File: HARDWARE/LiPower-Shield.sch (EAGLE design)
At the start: 42 parts, among them U1 MAX17043G+U, U2 TPS61200, U3 MCP73831, U4 ARDUINO_SHIELDNOLABELS, X1 USBSMD

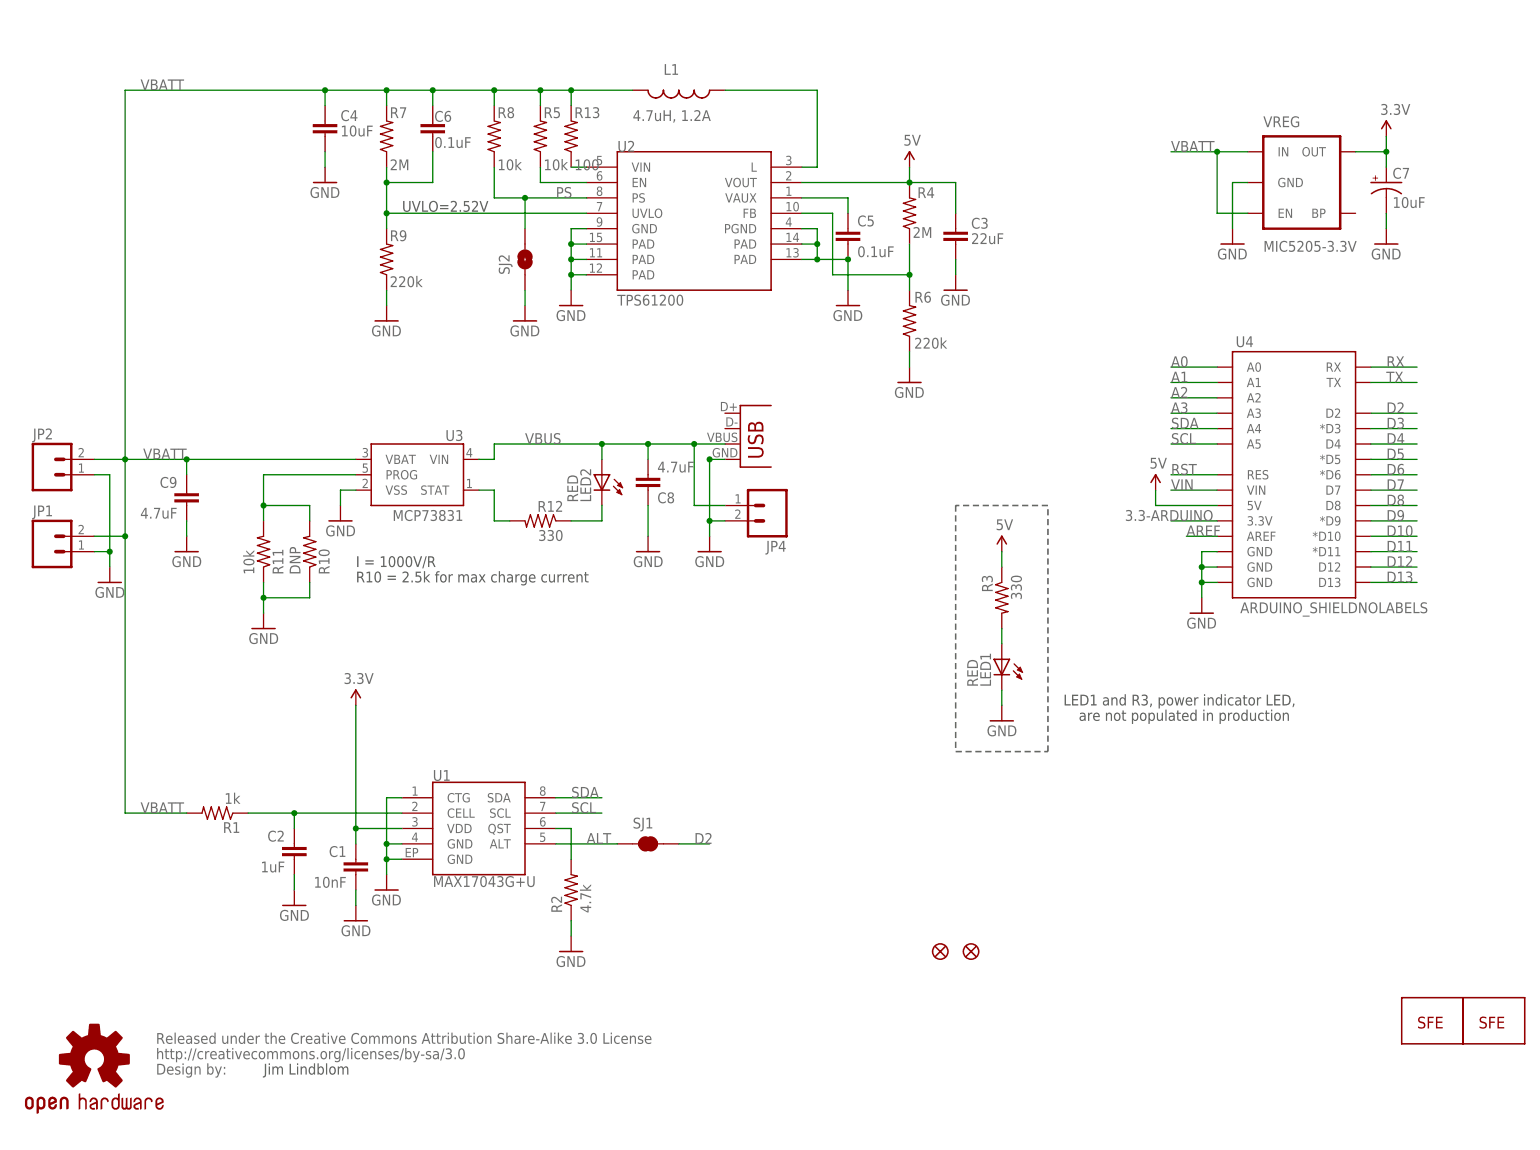
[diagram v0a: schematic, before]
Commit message: Had to re-commit original files
The v13 files that I pulled from the network are not what we have on
storefront. commited v12,  also from the network, seems to be the same
as the SF product.
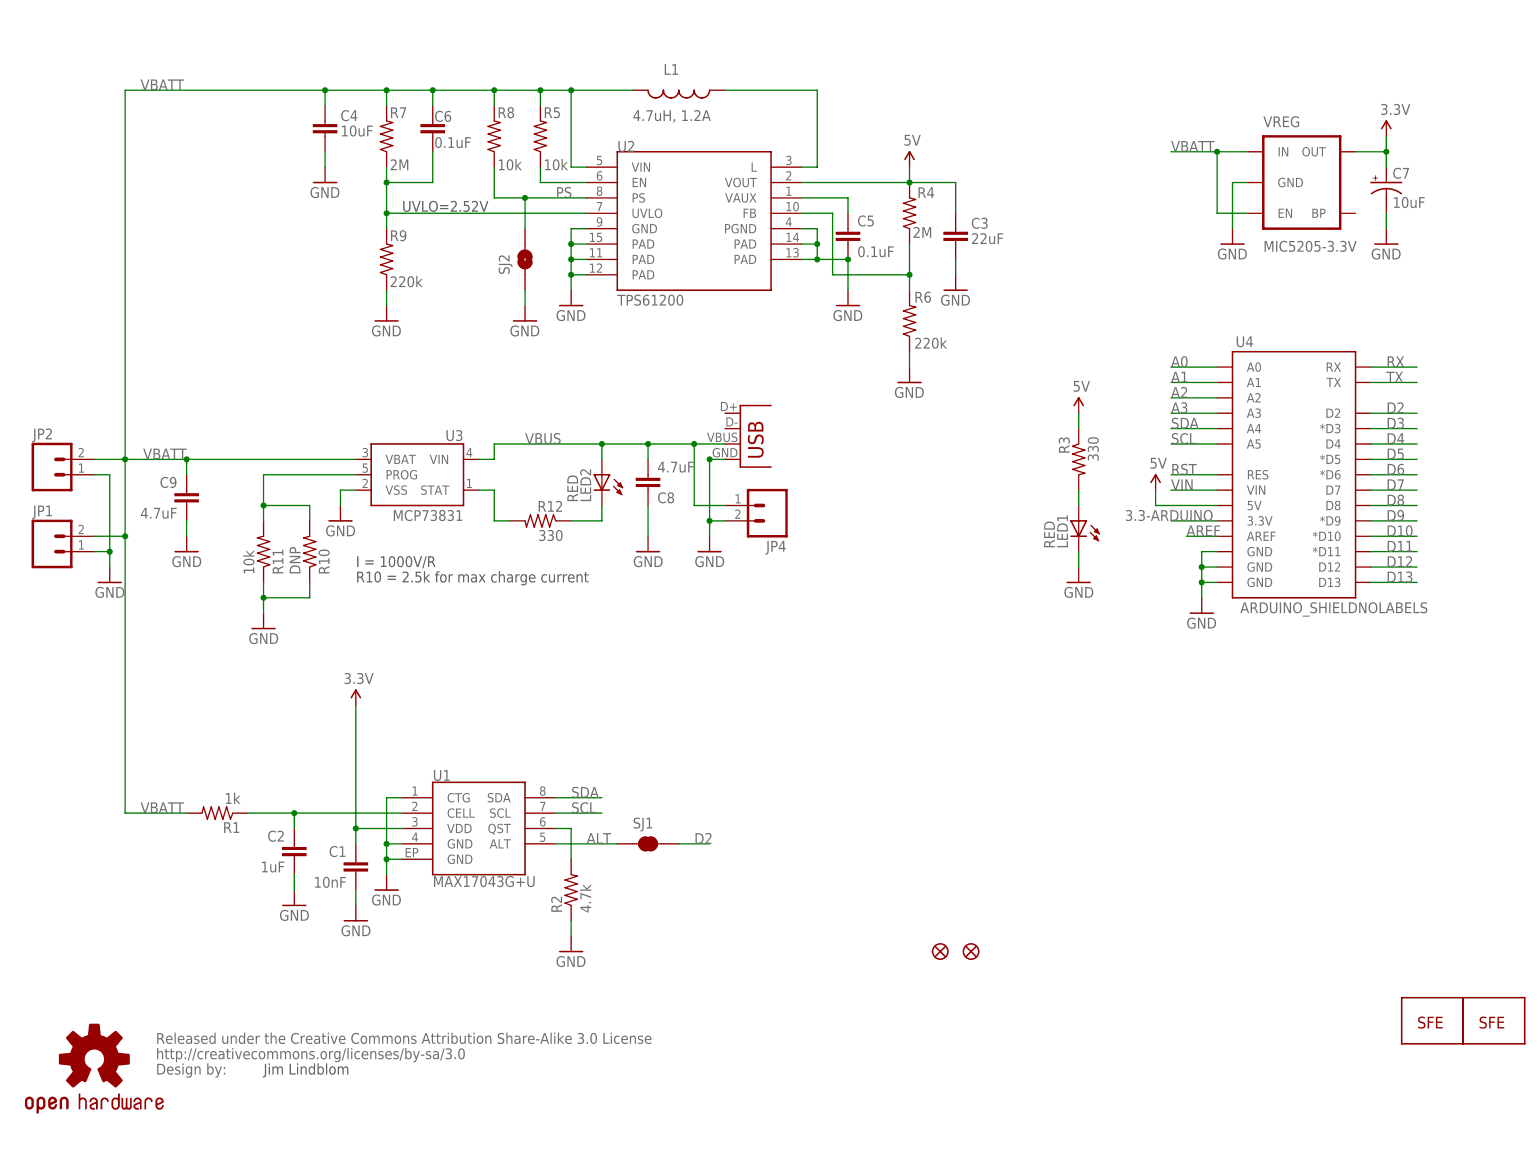
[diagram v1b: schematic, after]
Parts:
- removed R13: 100, SparkFun:RESISTOR0402-RES
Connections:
- removed net VIN-L: R13.1, U2.VIN
- net VBATT: now also U2.VIN; no longer R13.2
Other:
- note removed: "LED1 and R3, power indicator LED,"
- note removed: "are not populated in production"
- moved on the sheet: LED1, R3
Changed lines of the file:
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@@
 <part name="JP5" library="abes" deviceset="FIDUCIAL" device="1X2.5"/>
 <part name="JP6" library="abes" deviceset="FIDUCIAL" device="1X2.5"/>
-<part name="R13" library="SparkFun" deviceset="RESISTOR" device="0402-RES" value="100"/>
 </parts>
 <sheets>
@@
 <plain>
 <wire x1="103.124" y1="48.26" x2="105.156" y2="48.26" width="1.27" layer="94"/>
-<wire x1="154.94" y1="104.14" x2="154.94" y2="63.5" width="0.254" layer="97" style="shortdash"/>
-<wire x1="154.94" y1="63.5" x2="170.18" y2="63.5" width="0.254" layer="97" style="shortdash"/>
-<wire x1="170.18" y1="63.5" x2="170.18" y2="104.14" width="0.254" layer="97" style="shortdash"/>
-<wire x1="170.18" y1="104.14" x2="154.94" y2="104.14" width="0.254" layer="97" style="shortdash"/>
 <text x="40.64" y="10.16" size="1.778" layer="97">Jim Lindblom</text>
 <text x="55.88" y="93.98" size="1.778" layer="97">I = 1000V/R</text>
 <text x="55.88" y="91.44" size="1.778" layer="97">R10 = 2.5k for max charge current</text>
 <text x="63.5" y="152.654" size="1.778" layer="97">UVLO=2.52V</text>
-<text x="172.72" y="71.12" size="1.778" layer="97">LED1 and R3, power indicator LED,</text>
-<text x="175.26" y="68.58" size="1.778" layer="97">are not populated in production</text>
 </plain>
 <instances>
@@
 <instance part="C2" gate="G$1" x="45.72" y="45.72" rot="MR0"/>
 <instance part="GND11" gate="1" x="45.72" y="38.1" rot="MR0"/>
-<instance part="LED1" gate="G$1" x="162.56" y="78.74" rot="MR0"/>
-<instance part="R3" gate="G$1" x="162.56" y="88.9" rot="MR270"/>
-<instance part="U$5" gate="G$1" x="162.56" y="96.52"/>
-<instance part="GND14" gate="1" x="162.56" y="68.58" rot="MR0"/>
+<instance part="LED1" gate="G$1" x="175.26" y="101.6" rot="MR0"/>
+<instance part="R3" gate="G$1" x="175.26" y="111.76" rot="MR270"/>
+<instance part="U$5" gate="G$1" x="175.26" y="119.38"/>
+<instance part="GND14" gate="1" x="175.26" y="91.44" rot="MR0"/>
 <instance part="C3" gate="G$1" x="154.94" y="147.32" smashed="yes">
 <attribute name="NAME" x="157.48" y="149.86" size="1.778" layer="95"/>
@@
 <instance part="JP5" gate="G$1" x="152.4" y="30.48"/>
 <instance part="JP6" gate="G$1" x="157.48" y="30.48"/>
-<instance part="R13" gate="G$1" x="91.44" y="165.1" smashed="yes" rot="R90">
-<attribute name="NAME" x="91.948" y="168.1226" size="1.778" layer="95"/>
-<attribute name="VALUE" x="91.948" y="159.512" size="1.778" layer="96"/>
-</instance>
 </instances>
 <busses>
@@
 </segment>
 <segment>
-<wire x1="162.56" y1="71.12" x2="162.56" y2="73.66" width="0.1524" layer="91"/>
+<wire x1="175.26" y1="93.98" x2="175.26" y2="96.52" width="0.1524" layer="91"/>
 <pinref part="LED1" gate="G$1" pin="C"/>
 <pinref part="GND14" gate="1" pin="GND"/>
@@
 </segment>
 <segment>
-<wire x1="162.56" y1="96.52" x2="162.56" y2="93.98" width="0.1524" layer="91"/>
+<wire x1="175.26" y1="119.38" x2="175.26" y2="116.84" width="0.1524" layer="91"/>
 <pinref part="R3" gate="G$1" pin="1"/>
 <pinref part="U$5" gate="G$1" pin="5V"/>
@@
 <wire x1="60.96" y1="170.18" x2="60.96" y2="172.72" width="0.1524" layer="91"/>
 <wire x1="50.8" y1="170.18" x2="50.8" y2="172.72" width="0.1524" layer="91"/>
+<wire x1="50.8" y1="172.72" x2="60.96" y2="172.72" width="0.1524" layer="91"/>
+<wire x1="60.96" y1="172.72" x2="68.58" y2="172.72" width="0.1524" layer="91"/>
+<wire x1="68.58" y1="170.18" x2="68.58" y2="172.72" width="0.1524" layer="91"/>
+<wire x1="68.58" y1="172.72" x2="78.74" y2="172.72" width="0.1524" layer="91"/>
+<wire x1="78.74" y1="172.72" x2="86.36" y2="172.72" width="0.1524" layer="91"/>
+<wire x1="86.36" y1="172.72" x2="91.44" y2="172.72" width="0.1524" layer="91"/>
+<wire x1="101.6" y1="172.72" x2="91.44" y2="172.72" width="0.1524" layer="91"/>
+<wire x1="91.44" y1="172.72" x2="91.44" y2="160.02" width="0.1524" layer="91"/>
+<wire x1="93.98" y1="160.02" x2="91.44" y2="160.02" width="0.1524" layer="91"/>
+<wire x1="78.74" y1="170.18" x2="78.74" y2="172.72" width="0.1524" layer="91"/>
 <wire x1="27.94" y1="53.34" x2="17.78" y2="53.34" width="0.1524" layer="91"/>
-<wire x1="12.7" y1="99.06" x2="17.78" y2="99.06" width="0.1524" layer="91"/>
-<wire x1="17.78" y1="99.06" x2="17.78" y2="53.34" width="0.1524" layer="91"/>
 <wire x1="55.88" y1="111.76" x2="27.94" y2="111.76" width="0.1524" layer="91"/>
 <wire x1="27.94" y1="111.76" x2="27.94" y2="109.22" width="0.1524" layer="91"/>
@@
 <wire x1="17.78" y1="111.76" x2="27.94" y2="111.76" width="0.1524" layer="91"/>
 <wire x1="17.78" y1="111.76" x2="17.78" y2="99.06" width="0.1524" layer="91"/>
+<wire x1="12.7" y1="99.06" x2="17.78" y2="99.06" width="0.1524" layer="91"/>
+<wire x1="17.78" y1="99.06" x2="17.78" y2="53.34" width="0.1524" layer="91"/>
 <wire x1="17.78" y1="111.76" x2="17.78" y2="172.72" width="0.1524" layer="91"/>
 <wire x1="17.78" y1="172.72" x2="50.8" y2="172.72" width="0.1524" layer="91"/>
-<wire x1="50.8" y1="172.72" x2="60.96" y2="172.72" width="0.1524" layer="91"/>
-<wire x1="60.96" y1="172.72" x2="68.58" y2="172.72" width="0.1524" layer="91"/>
-<wire x1="68.58" y1="170.18" x2="68.58" y2="172.72" width="0.1524" layer="91"/>
-<wire x1="68.58" y1="172.72" x2="78.74" y2="172.72" width="0.1524" layer="91"/>
-<wire x1="78.74" y1="170.18" x2="78.74" y2="172.72" width="0.1524" layer="91"/>
-<wire x1="78.74" y1="172.72" x2="86.36" y2="172.72" width="0.1524" layer="91"/>
-<wire x1="101.6" y1="172.72" x2="91.44" y2="172.72" width="0.1524" layer="91"/>
-<wire x1="91.44" y1="172.72" x2="86.36" y2="172.72" width="0.1524" layer="91"/>
 <wire x1="86.36" y1="170.18" x2="86.36" y2="172.72" width="0.1524" layer="91"/>
-<wire x1="91.44" y1="170.18" x2="91.44" y2="172.72" width="0.1524" layer="91"/>
-<junction x="17.78" y="99.06"/>
-<junction x="27.94" y="111.76"/>
-<junction x="17.78" y="111.76"/>
 <junction x="50.8" y="172.72"/>
 <junction x="60.96" y="172.72"/>
 <junction x="68.58" y="172.72"/>
+<junction x="91.44" y="172.72"/>
 <junction x="78.74" y="172.72"/>
+<junction x="27.94" y="111.76"/>
+<junction x="17.78" y="111.76"/>
+<junction x="17.78" y="99.06"/>
 <junction x="86.36" y="172.72"/>
-<junction x="91.44" y="172.72"/>
 <label x="20.32" y="172.72" size="1.778" layer="95"/>
 <label x="27.94" y="111.76" size="1.778" layer="95" rot="MR0"/>
@@
 <pinref part="R7" gate="G$1" pin="2"/>
 <pinref part="C4" gate="G$1" pin="1"/>
+<pinref part="C6" gate="G$1" pin="1"/>
+<pinref part="L1" gate="G$1" pin="2"/>
+<pinref part="U2" gate="G$1" pin="VIN"/>
+<pinref part="R8" gate="G$1" pin="2"/>
 <pinref part="R1" gate="G$1" pin="2"/>
-<pinref part="JP1" gate="G$1" pin="2"/>
 <pinref part="C9" gate="G$1" pin="1"/>
 <pinref part="U3" gate="G$1" pin="VBAT"/>
 <pinref part="JP2" gate="G$1" pin="2"/>
-<pinref part="C6" gate="G$1" pin="1"/>
-<pinref part="R8" gate="G$1" pin="2"/>
-<pinref part="L1" gate="G$1" pin="2"/>
+<pinref part="JP1" gate="G$1" pin="2"/>
 <pinref part="R5" gate="G$1" pin="2"/>
-<pinref part="R13" gate="G$1" pin="2"/>
 </segment>
 </net>
@@
 <net name="N$1" class="0">
 <segment>
-<wire x1="162.56" y1="83.82" x2="162.56" y2="81.28" width="0.1524" layer="91"/>
+<wire x1="175.26" y1="106.68" x2="175.26" y2="104.14" width="0.1524" layer="91"/>
 <pinref part="LED1" gate="G$1" pin="A"/>
 <pinref part="R3" gate="G$1" pin="2"/>
@@
 </segment>
 </net>
-<net name="VIN-L" class="0">
-<segment>
-<wire x1="93.98" y1="160.02" x2="91.44" y2="160.02" width="0.1524" layer="91"/>
-<pinref part="U2" gate="G$1" pin="VIN"/>
-<pinref part="R13" gate="G$1" pin="1"/>
-</segment>
-</net>

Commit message: Computer Change
0603 updated, r3 update.  JST update, trace rework and schematic
cleanup.
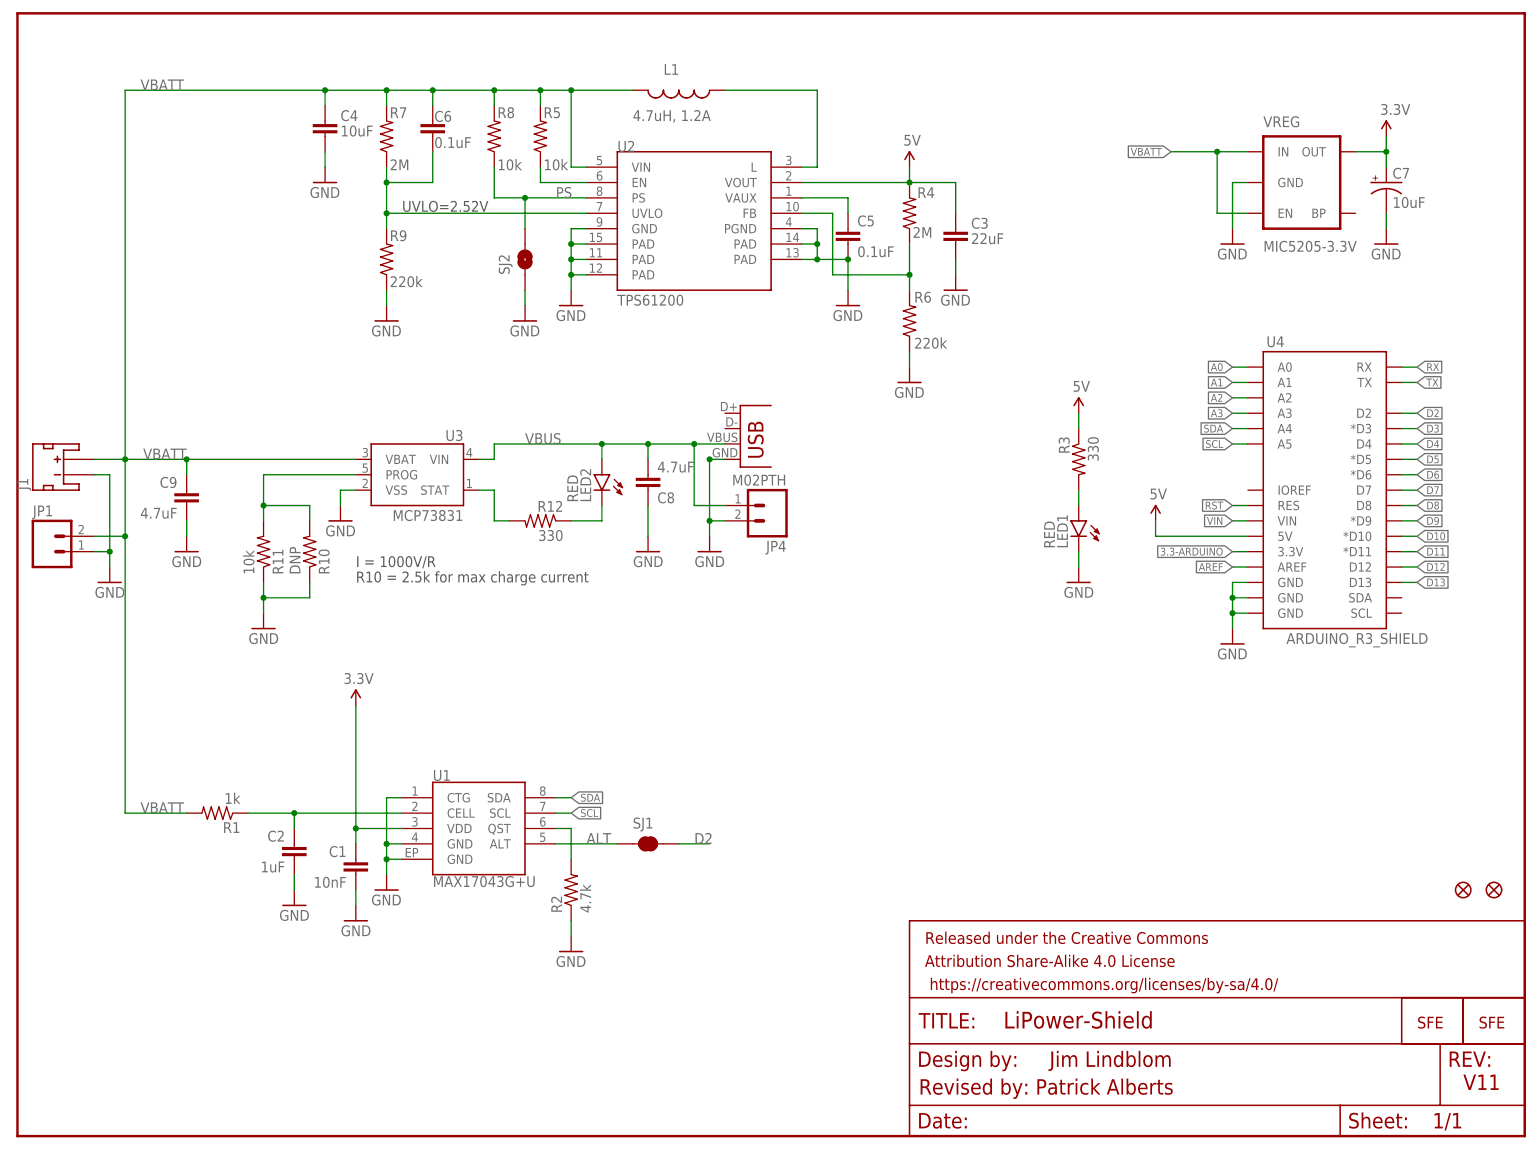
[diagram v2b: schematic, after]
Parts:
- removed $$U$1: CREATIVE_COMMONS, SparkFun:CREATIVE_COMMONS
- removed JP2: (no value), SparkFun:M02-JST-2MM-SMT
- removed U$100: OSHW-LOGOM, SparkFun:OSHW-LOGOM
- added FRAME1: FRAME-LETTER, SparkFun-Aesthetics:FRAME-LETTER
- added J1: (no value), SparkFun-Connectors:JST_2MM_MALE
- C1: device SparkFun:CAP0402-CAP -> SparkFun-Capacitors:10NF/10000PF-50V-10%(0603)
- C2: device SparkFun:CAP0402-CAP -> SparkFun-Capacitors:1.0UF-16V-10%(0603)
- C5, C6: device SparkFun:CAP0402-CAP -> SparkFun-Capacitors:0.1UF-25V(+80/-20%)(0603)
- C8, C9: device SparkFun:CAP0402-CAP -> SparkFun-Capacitors:4.7UF-6.3V-10%(0603)0603
- JP4: value (none) -> M02PTH; device SparkFun:M021X02_NO_SILK -> SparkFun-Connectors:M02PTH
- LED1, LED2: device SparkFun:LED0603 -> SparkFun-LED:LED-RED0603
- R1: device SparkFun:RESISTOR0402-RES -> SparkFun-Resistors:1KOHM1/10W1%(0603)
- R10: device SparkFun:RESISTORPTH-1/6W -> SparkFun-Resistors:RESISTORPTH-1/6W
- R11, R5, R8: device SparkFun:RESISTOR0402-RES -> SparkFun-Resistors:10KOHM1/10W1%(0603)0603
- R12, R3: device SparkFun:RESISTOR0402-RES -> SparkFun-Resistors:330OHM1/10W1%(0603)
- R2: device SparkFun:RESISTOR0402-RES -> SparkFun-Resistors:4.7KOHM1/10W1%(0603)
- R4, R7: device SparkFun:RESISTOR0402-RES -> SparkFun-Resistors:2MOHMS-1/10W-1%(0603)
- R6, R9: device SparkFun:RESISTOR0402-RES -> SparkFun-Resistors:220KOHM1/10W1%(0603)
- U4: value ARDUINO_SHIELDNOLABELS -> ARDUINO_R3_SHIELD; device SparkFun:ARDUINO_SHIELDNOLABELS -> SparkFun-Boards:ARDUINO_R3_SHIELD
- X1: device SparkFun:USBSMD -> SparkFun-Connectors:USBSMD
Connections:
- net GND: now also J1.-; no longer JP2.1
- net VBATT: now also J1.+; no longer JP2.2
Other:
- note added: "Revised by: Patrick Alberts"
- note added: "V11"

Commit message: Added OSHW, SPK Logo
Also added flags to schematic
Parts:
- removed JP3: LOGO-SFENW2, SparkFun:LOGO-SFENW2
- added LOGO1: OSHW-LOGOS, SparkFun-Aesthetics:OSHW-LOGOS
- added LOGO2: SFE_LOGO_NAME_FLAME.2_INCH, SparkFun-Aesthetics:SFE_LOGO_NAME_FLAME.2_INCH
- added TP1: TEST-POINT3X5, SparkFun-Passives:TEST-POINT3X5
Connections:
- net UVLO: now also TP1.1
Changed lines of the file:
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@@
 <part name="P+8" library="SparkFun" deviceset="3.3V" device=""/>
 <part name="JP1" library="SparkFun" deviceset="M02" device="1X02_NO_SILK"/>
-<part name="JP3" library="SparkFun" deviceset="LOGO-SFE" device="NW2"/>
 <part name="SJ1" library="SparkFun" deviceset="SOLDERJUMPER" device="TRACE"/>
 <part name="JP100" library="SparkFun" deviceset="LOGO-SFE" device="SK"/>
@@
 <part name="JP6" library="abes" deviceset="FIDUCIAL" device="1X2.5"/>
 <part name="J1" library="SparkFun-Connectors" deviceset="JST_2MM_MALE" device=""/>
+<part name="TP1" library="SparkFun-Passives" deviceset="TEST-POINT" device="3X5"/>
+<part name="LOGO1" library="SparkFun-Aesthetics" deviceset="OSHW-LOGO" device="S"/>
+<part name="LOGO2" library="SparkFun-Aesthetics" deviceset="SFE_LOGO_NAME_FLAME" device=".2_INCH" value="SFE_LOGO_NAME_FLAME.2_INCH"/>
 </parts>
 <sheets>
@@
 <instance part="P+8" gate="G$1" x="226.06" y="165.1"/>
 <instance part="JP1" gate="G$1" x="5.08" y="96.52"/>
-<instance part="JP3" gate="G$1" x="241.3" y="17.78"/>
 <instance part="SJ1" gate="1" x="104.14" y="48.26" smashed="yes">
 <attribute name="NAME" x="101.6" y="50.8" size="1.778" layer="95"/>
@@
 <instance part="JP6" gate="G$1" x="238.76" y="40.64"/>
 <instance part="J1" gate="G$1" x="7.62" y="109.22" rot="R90"/>
+<instance part="TP1" gate="G$1" x="43.18" y="152.4" rot="R180"/>
+<instance part="LOGO1" gate="G$1" x="220.98" y="48.26"/>
+<instance part="LOGO2" gate="G$1" x="149.86" y="35.56"/>
 </instances>
 <busses>
@@
 <pinref part="R7" gate="G$1" pin="1"/>
 <pinref part="R9" gate="G$1" pin="2"/>
-</segment>
-</net>
+<pinref part="TP1" gate="G$1" pin="1"/>
+<wire x1="43.18" y1="152.4" x2="60.96" y2="152.4" width="0.1524" layer="91"/>
+</segment>
+</net>
